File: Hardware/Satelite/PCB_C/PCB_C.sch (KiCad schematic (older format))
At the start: 46 parts, among them J1 SWD, J3 Conector_PCB_B-C, J4 Conector_Expansion_CanSat, J5 USB_B_Micro, M1 Spacer, M2 Spacer, M3 Spacer, U1 TXS0104ERGYR, U2 TCA9802DGKR, U3 W25Q32JVSSIQ, U4 TXS0104ERGYR, U5 BL654, U7 Si7051-A20, Y1 LFXTAL016178

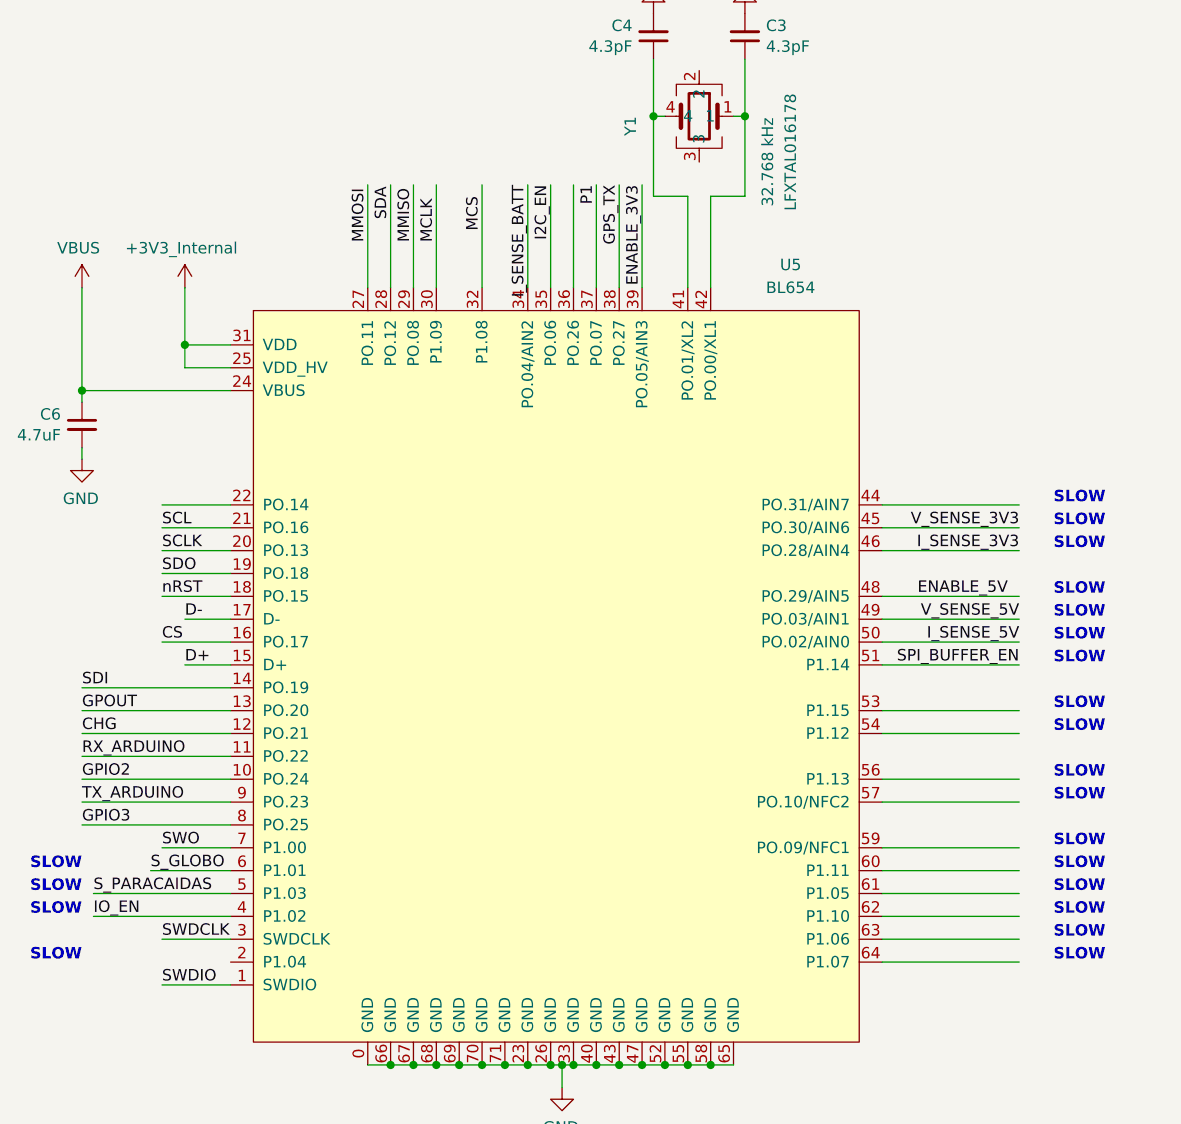
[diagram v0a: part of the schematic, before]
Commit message: Corrección del pin nRST mal ubicado en PCB_C
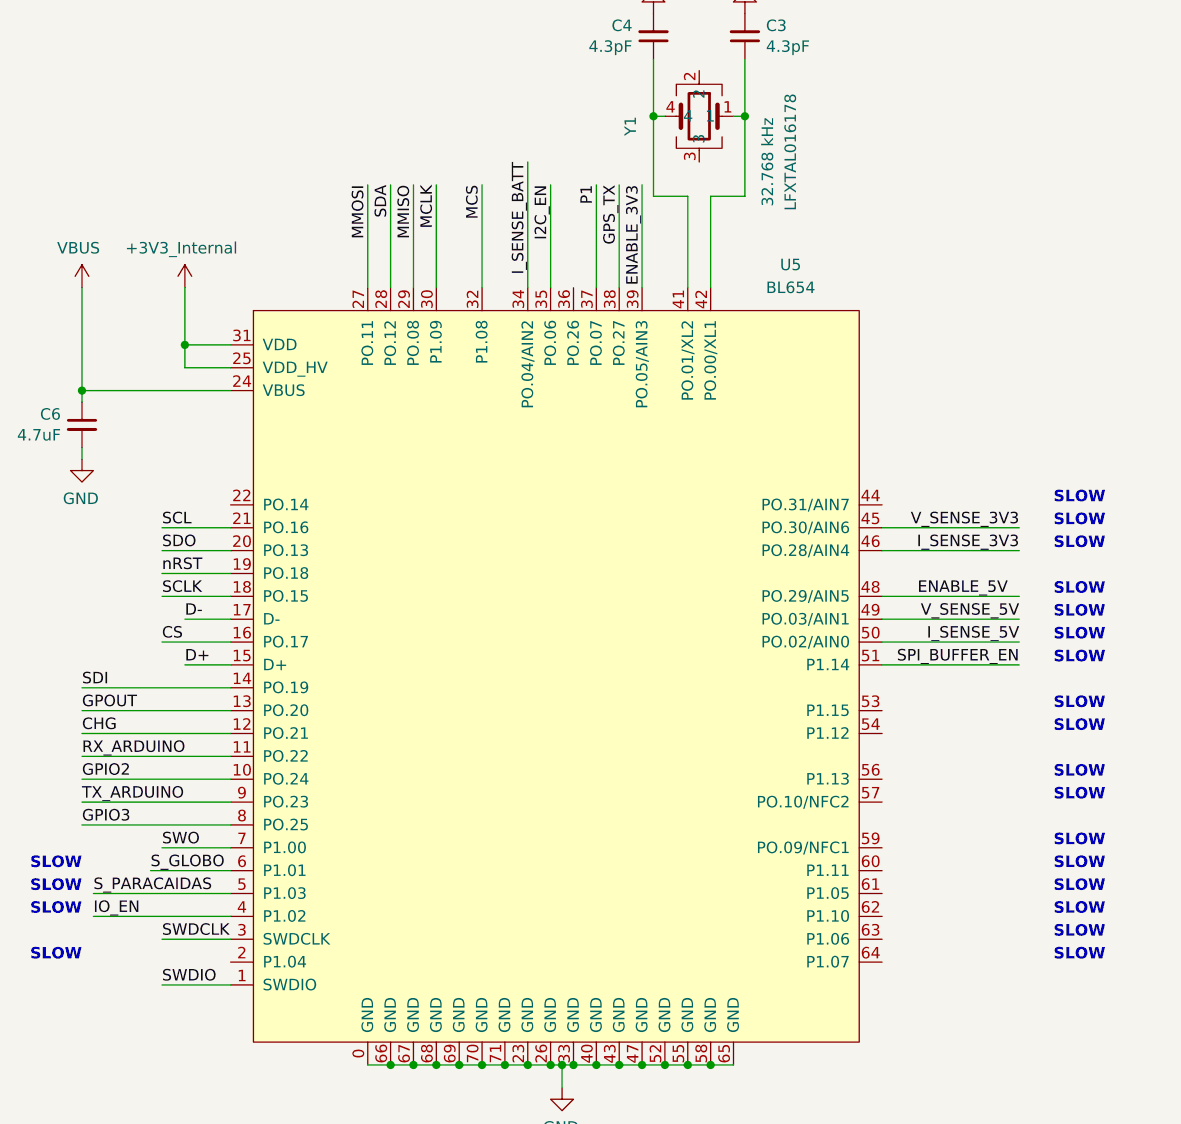
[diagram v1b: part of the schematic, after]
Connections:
- wire segments 316 -> 303
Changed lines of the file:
@@
 Text Label 10250 4050 2    50   ~ 0
 V_SENSE_5V
-Text Label 8100 2150 3    50   ~ 0
+Text Label 8100 2050 3    50   ~ 0
 I_SENSE_BATT
 Text Label 10200 3950 2    50   ~ 0
@@
 Text Label 6150 4550 0    50   ~ 0
 CHG
-Text Label 6500 3850 0    50   ~ 0
+Text Label 6500 3750 0    50   ~ 0
 SDO
 Text Label 6150 4350 0    50   ~ 0
 SDI
-Text Label 6500 3750 0    50   ~ 0
+Text Label 6500 3950 0    50   ~ 0
 SCLK
 Text Label 6500 4150 0    50   ~ 0
@@
 $EndComp
 Wire Wire Line
-	9650 3550 10250 3550
-Wire Wire Line
 	9650 3950 10250 3950
 Wire Wire Line
-	9650 4450 10250 4450
-Wire Wire Line
-	9650 4750 10250 4750
-Wire Wire Line
-	9650 5350 10250 5350
-Wire Wire Line
 	9650 3650 10250 3650
 Wire Wire Line
@@
 Wire Wire Line
 	9650 4050 10250 4050
-Wire Wire Line
-	9650 4550 10250 4550
-Wire Wire Line
-	9650 5150 10250 5150
-Wire Wire Line
-	9650 4850 10250 4850
-Wire Wire Line
-	9650 5050 10250 5050
-Wire Wire Line
-	9650 5250 10250 5250
 $Comp
 L power:GND #PWR015
@@
 Wire Wire Line
 	9650 4150 10250 4150
-Text Label 7500 2300 1    50   ~ 0
+Text Label 7500 2150 3    50   ~ 0
 SDA
 Wire Wire Line
@@
 Wire Wire Line
 	6800 5050 6500 5050
-Text Label 6500 3950 0    50   ~ 0
+Text Label 6500 3850 0    50   ~ 0
 nRST
 Wire Wire Line
@@
 Text Label 7150 7000 0    50   ~ 0
 MCS
-Text Label 7900 2350 1    50   ~ 0
+Text Label 7900 2150 3    50   ~ 0
 MCS
-Text Label 7600 2400 1    50   ~ 0
+Text Label 7600 2150 3    50   ~ 0
 MMISO
-Text Label 7400 2400 1    50   ~ 0
+Text Label 7400 2150 3    50   ~ 0
 MMOSI
-Text Label 7700 2400 1    50   ~ 0
+Text Label 7700 2150 3    50   ~ 0
 MCLK
 Wire Wire Line
@@
 GPIO3
 Wire Wire Line
-	8100 2150 8100 2600
+	8100 2050 8100 2600
 Wire Wire Line
 	8200 2150 8200 2600
@@
 ENABLE_3V3
 Wire Wire Line
-	9650 5450 10250 5450
-Wire Wire Line
-	9650 5550 10250 5550
-Wire Wire Line
 	7900 2600 7900 2150
-Wire Wire Line
-	8300 2150 8300 2600
 Text Label 6500 3650 0    50   ~ 0
 SCL
@@
 	6800 3650 6500 3650
 Wire Wire Line
-	6800 3550 6500 3550
-Wire Wire Line
 	6150 3350 6150 3300

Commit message: Nuevos conectores micro-usb completamente SMD
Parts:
- J5: footprint Connector_USB:USB_Micro-B_Molex-105017-0001 -> Connector_USB:USB_Micro-B_Molex_47346-0001; Manufacturer Part Number 105017-0001 -> 47346-1001
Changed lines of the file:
@@
 F 0 "J5" H 900 8250 50  0000 R CNN
 F 1 "USB_B_Micro" H 1050 8150 50  0000 R CNN
-F 2 "Connector_USB:USB_Micro-B_Molex-105017-0001" H 1000 7750 50  0001 C CNN
+F 2 "Connector_USB:USB_Micro-B_Molex_47346-0001" H 1000 7750 50  0001 C CNN
 F 3 "https://www.molex.com/webdocs/datasheets/pdf/en-us/1050170001_IO_CONNECTORS.pdf" H 1000 7750 50  0001 C CNN
-F 4 "105017-0001" H 850 7800 50  0001 C CNN "Manufacturer Part Number"
+F 4 "47346-1001" H 850 7800 50  0001 C CNN "Manufacturer Part Number"
 	1    850  7800
 	1    0    0    -1

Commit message: Corregido número de parte de conector B-C en PCB_C
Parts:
- J3: Manufacturer Part Number 53353-1071 -> 53353-2071; Notes Hecho con dos 53353-1071 y sus dos opuestos 52465-2071 -> Hecho con dos 53353-2071 y sus dos opuestos 52465-2071
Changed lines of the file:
@@
 F 2 "AXTEC:Conector_PCB_B-C_Lado_C" H 14150 2200 50  0001 C CNN
 F 3 "" H 14150 2200 50  0001 C CNN
-F 4 "Hecho con dos 53353-1071 y sus dos opuestos 52465-2071" H 0   -150 50  0001 C CNN "Notes"
-F 5 "53353-1071" H 14250 1450 50  0001 C CNN "Manufacturer Part Number"
+F 4 "Hecho con dos 53353-2071 y sus dos opuestos 52465-2071" H 0   -150 50  0001 C CNN "Notes"
+F 5 "53353-2071" H 14250 1450 50  0001 C CNN "Manufacturer Part Number"
 F 6 "2" H 14250 1450 50  0001 C CNN "Quantity"
 	1    14250 1450
